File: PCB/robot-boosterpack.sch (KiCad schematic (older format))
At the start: 33 parts

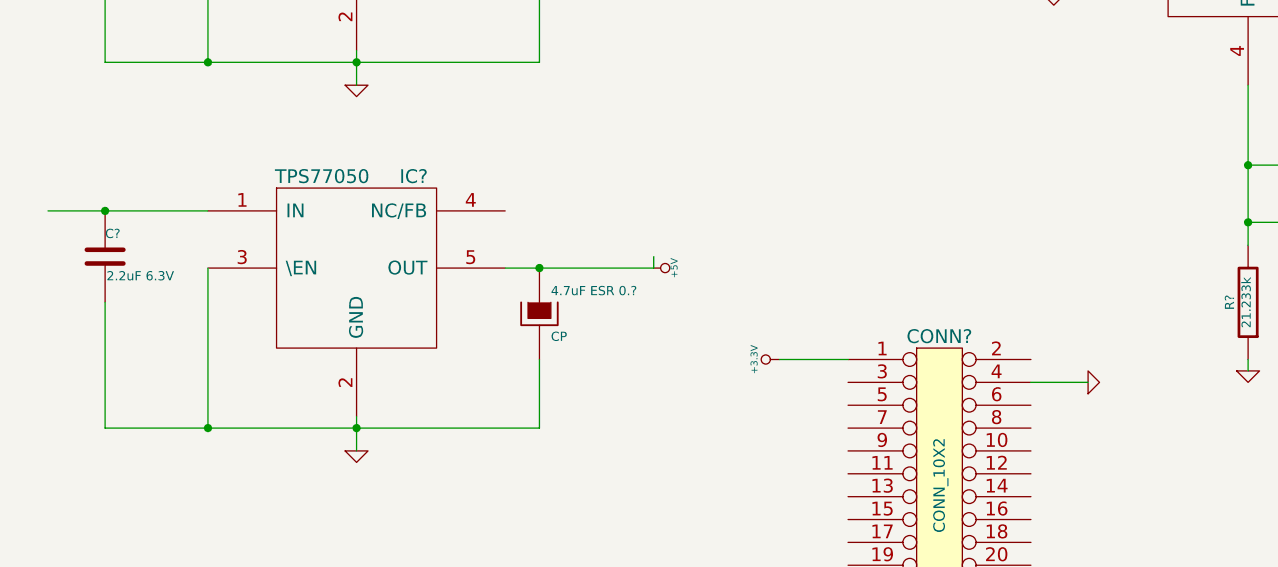
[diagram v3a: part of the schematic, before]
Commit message: updated 5V regulator circuit
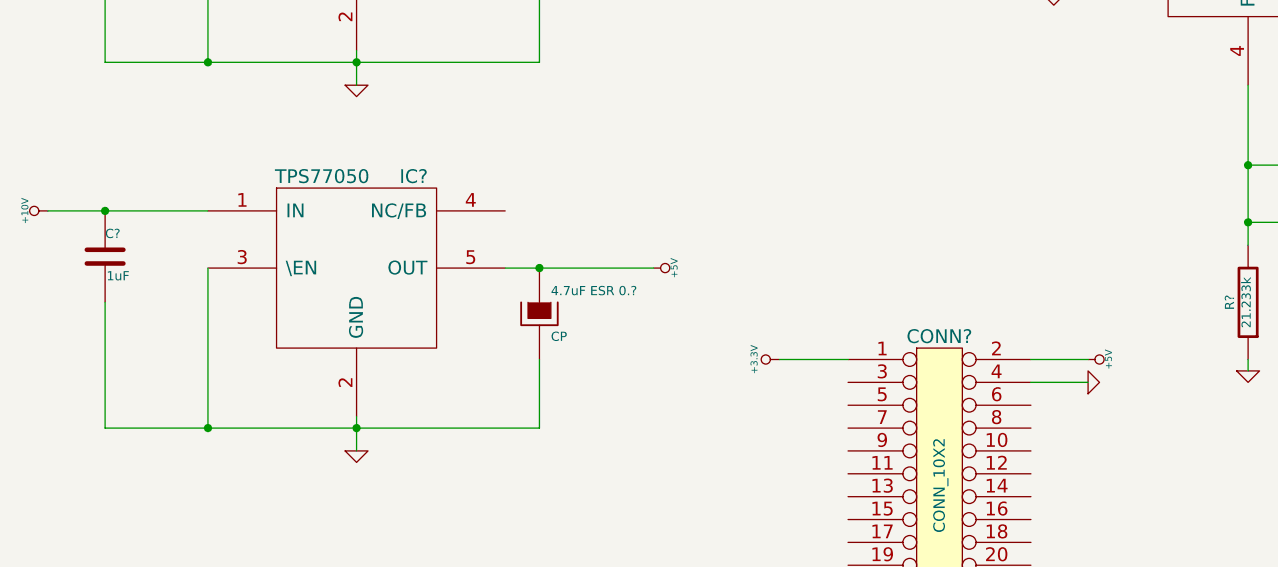
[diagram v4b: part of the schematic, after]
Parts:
- C?: value 2.2uF 6.3V -> 1uF
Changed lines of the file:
@@
 P 950 2700
 F 0 "C?" H 950 2800 40  0000 L CNN
-F 1 "2.2uF 6.3V" H 956 2615 40  0000 L CNN
+F 1 "1uF" H 956 2615 40  0000 L CNN
 F 2 "~" H 988 2550 30  0000 C CNN
 F 3 "~" H 950 2700 60  0000 C CNN
@@
 	0    1    1    0
 $EndComp
-Wire Wire Line
-	3350 2750 3350 2700
 Connection ~ 2850 2750
 Connection ~ 950  900
 Connection ~ 2850 1150
+$Comp
+L +5V #PWR?
+U 1 1 53AA0197
+P 5250 3150
+F 0 "#PWR?" H 5250 3240 20  0001 C CNN
+F 1 "+5V" H 5250 3240 30  0000 C CNN
+F 2 "" H 5250 3150 60  0000 C CNN
+F 3 "" H 5250 3150 60  0000 C CNN
+	1    5250 3150
+	0    1    1    0
+$EndComp
+Wire Wire Line
+	5000 3150 5250 3150
+$Comp
+L +10V #PWR?
+U 1 1 53AA074A
+P 700 2500
+F 0 "#PWR?" H 700 2450 20  0001 C CNN
+F 1 "+10V" H 700 2600 30  0000 C CNN
+F 2 "" H 700 2500 60  0000 C CNN
+F 3 "" H 700 2500 60  0000 C CNN
+	1    700  2500
+	0    -1   -1   0
+$EndComp
 $EndSCHEMATC

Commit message: updated 5V regulator capacitor values
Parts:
- removed 4.7uF~ESR~0.?: CP, symbol CP
- added C?: 4.7uF ESR 0.2, symbol CP
- C?: renamed from 4.7uF; value CP -> 4.7uF ESR 0.2
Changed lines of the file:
@@
 $EndComp
 $Comp
-L CP 4.7uF
+L CP C?
 U 1 1 53A8B338
 P 2850 1350
-F 0 "4.7uF ESR 0.2" H 2900 1450 40  0000 L CNN
-F 1 "CP" H 2900 1250 40  0000 L CNN
+F 0 "C?" H 2900 1450 40  0000 L CNN
+F 1 "4.7uF ESR 0.2" H 2900 1250 40  0000 L CNN
 F 2 "" H 2950 1200 30  0000 C CNN
 F 3 "" H 2850 1350 300 0000 C CNN
@@
 	1    0    0    -1
 $EndComp
-$Comp
-L CP 4.7uF~ESR~0.?
-U 1 1 53A9EE61
-P 2850 2950
-F 0 "4.7uF ESR 0.?" H 2900 3050 40  0000 L CNN
-F 1 "CP" H 2900 2850 40  0000 L CNN
-F 2 "" H 2950 2800 30  0000 C CNN
-F 3 "" H 2850 2950 300 0000 C CNN
-	1    2850 2950
-	1    0    0    -1
-$EndComp
 Wire Wire Line
 	1400 2500 700  2500
@@
 	0    -1   -1   0
 $EndComp
+$Comp
+L CP C?
+U 1 1 53AA20BE
+P 2850 2950
+F 0 "C?" H 2900 3050 40  0000 L CNN
+F 1 "4.7uF ESR 0.2" H 2900 2850 40  0000 L CNN
+F 2 "" H 2950 2800 30  0000 C CNN
+F 3 "" H 2850 2950 300 0000 C CNN
+	1    2850 2950
+	1    0    0    -1
+$EndComp
 $EndSCHEMATC

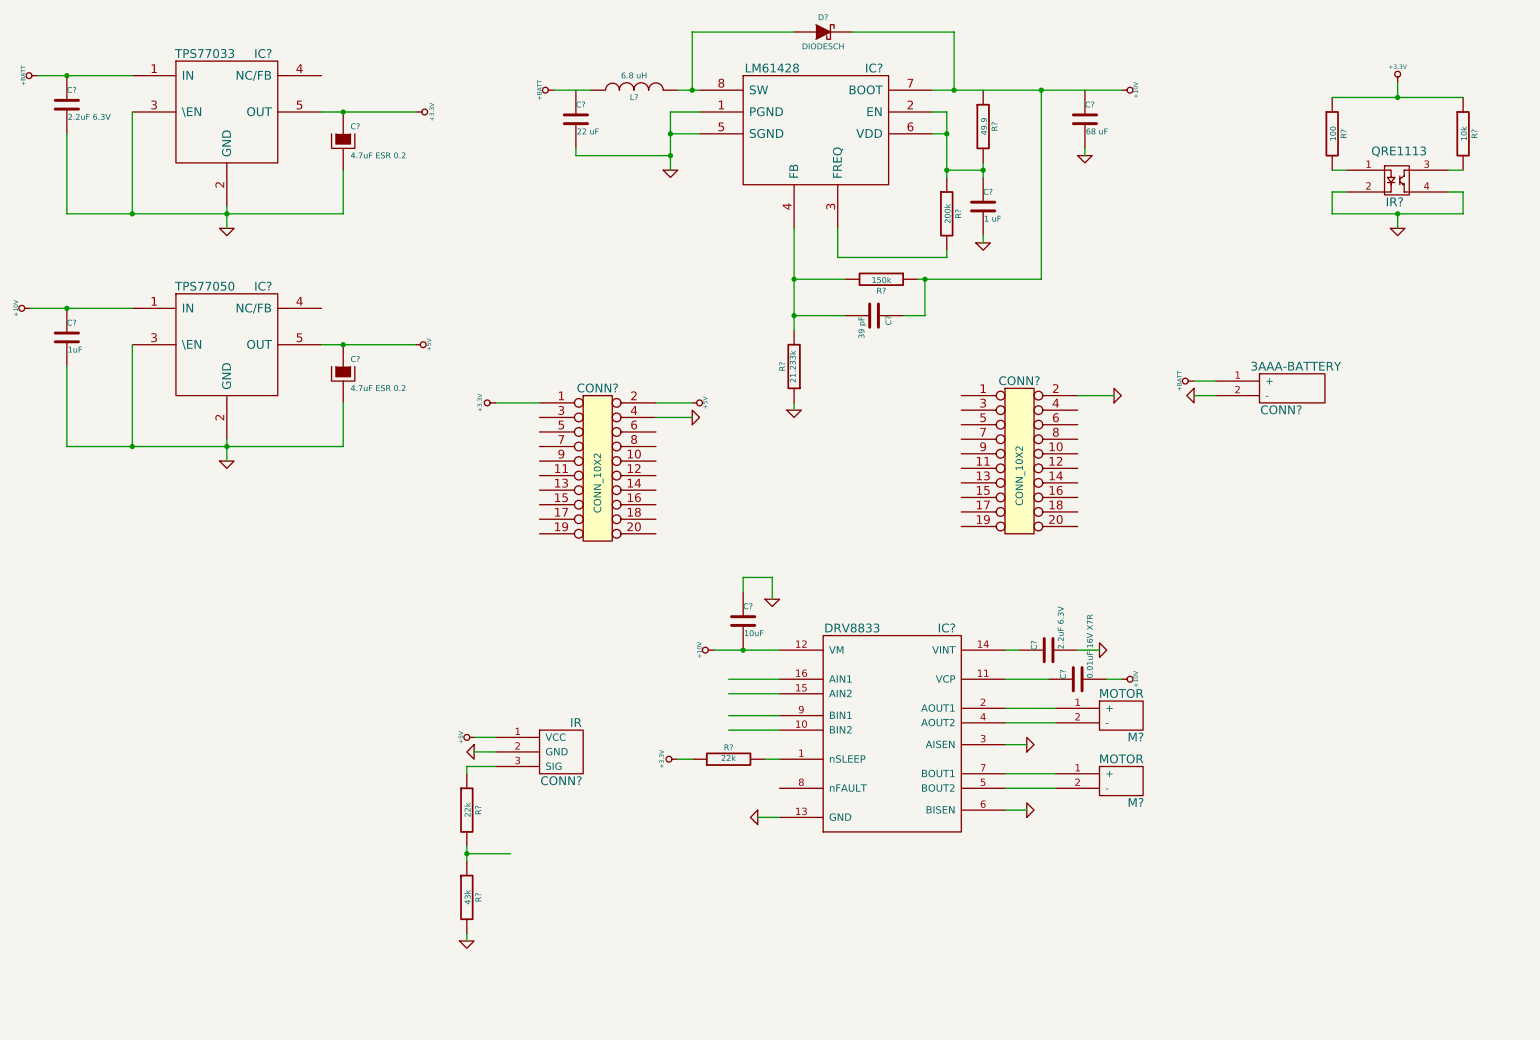
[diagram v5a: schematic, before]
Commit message: added servo connectors
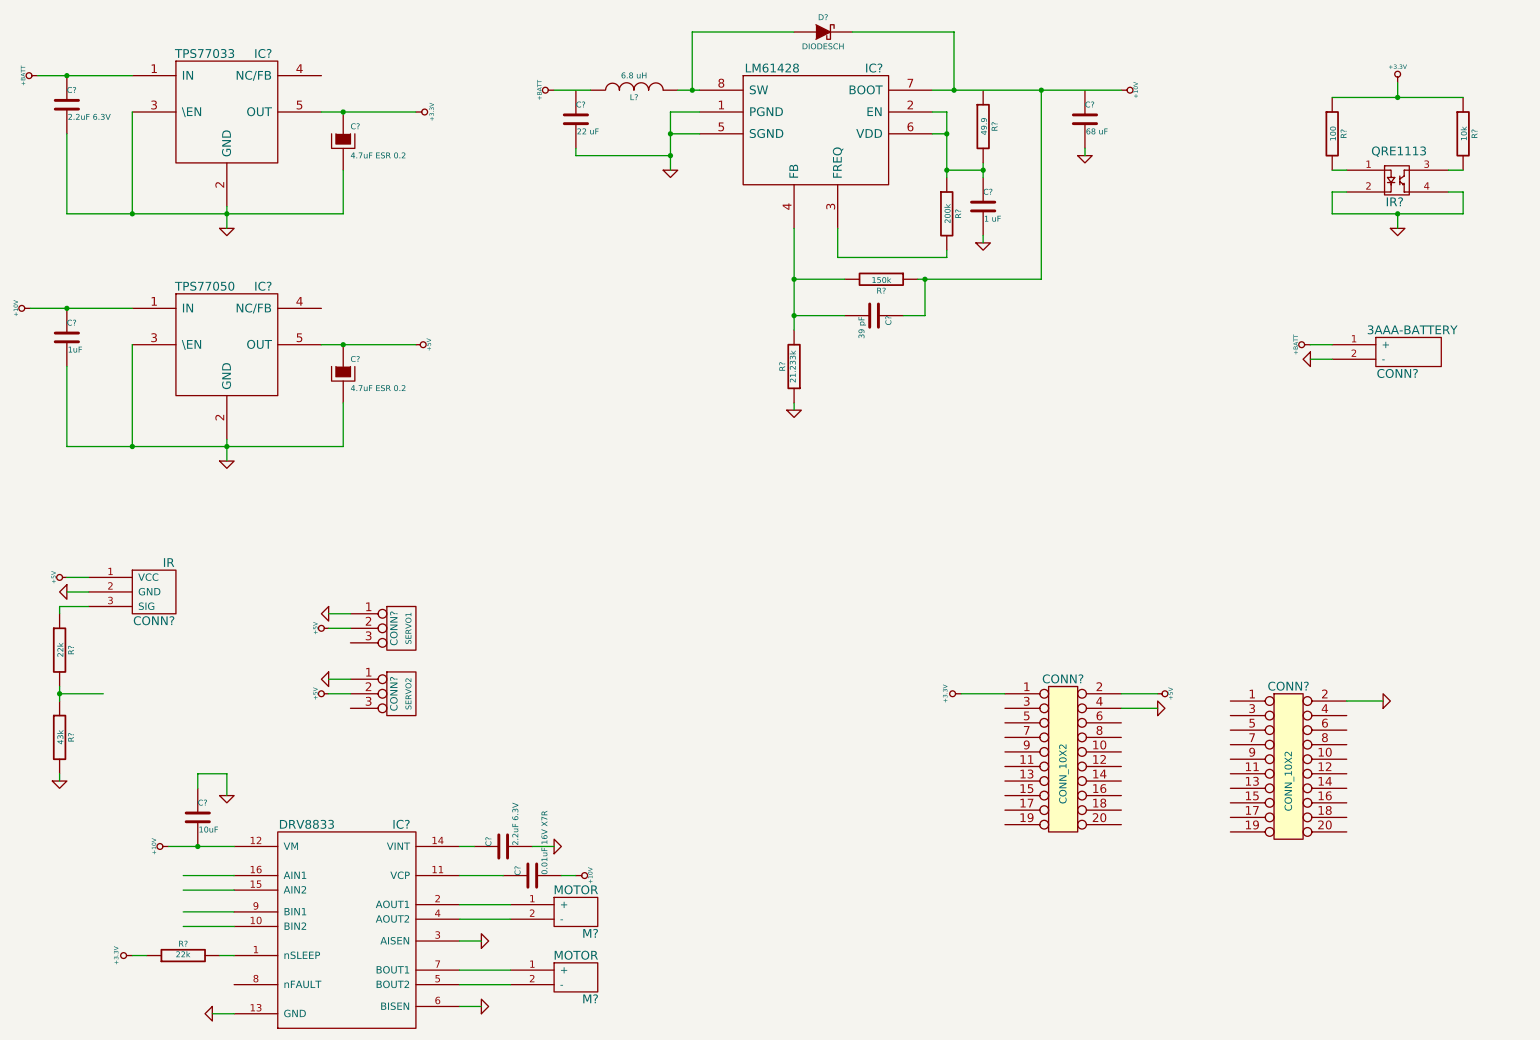
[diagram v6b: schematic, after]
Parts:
- added CONN?: SERVO2, symbol CONN_3
- added CONN?: SERVO1, symbol CONN_3
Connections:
- wire segments 88 -> 92
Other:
- moved on the sheet: C?, CONN?, IC?, M?, R?

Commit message: created boosterpack connections
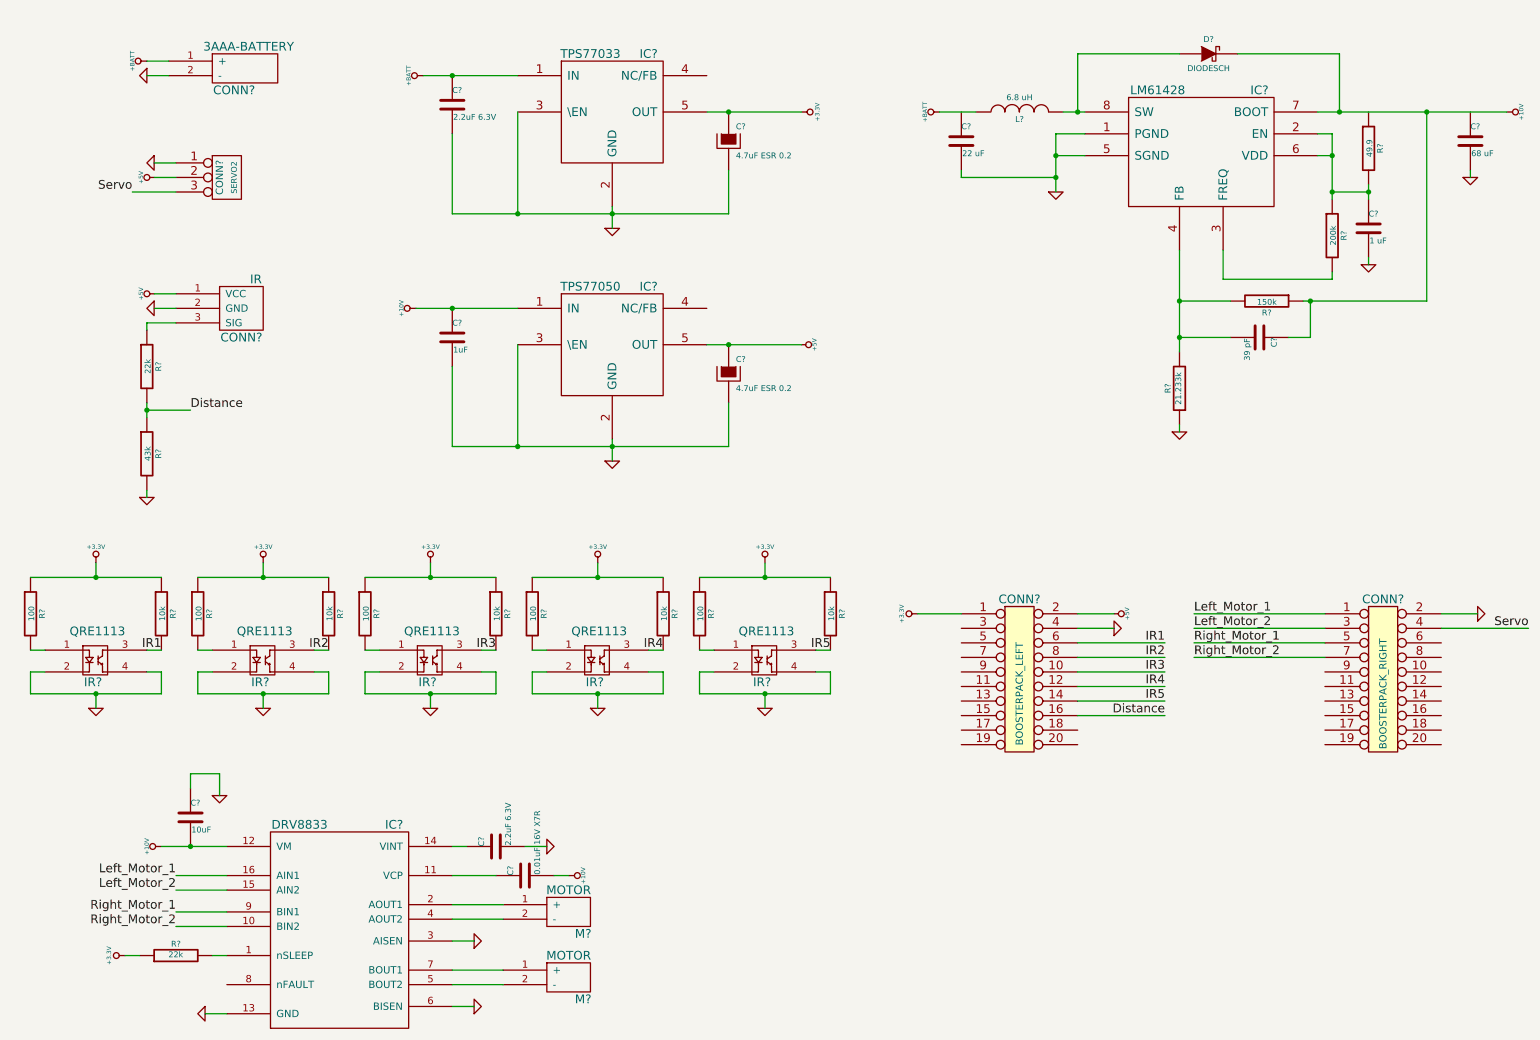
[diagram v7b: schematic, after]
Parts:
- removed CONN?: SERVO1, symbol CONN_3
- added IR? (x4): QRE1113, ~, symbol QRE1113
- added R? (x4): 100, ~, symbol R
- added R? (x4): 10k, ~, symbol R
- CONN?: value CONN_10X2 -> BOOSTERPACK_LEFT
- CONN?: value CONN_10X2 -> BOOSTERPACK_RIGHT
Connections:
- net labels added: Distance, IR1, IR2, IR3, IR4, IR5, Left_Motor_1, Left_Motor_2, Right_Motor_1, Right_Motor_2, Servo
- wire segments 92 -> 142
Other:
- moved on the sheet: C?, CONN?, D?, IC?, IR?, L?, M?, R?

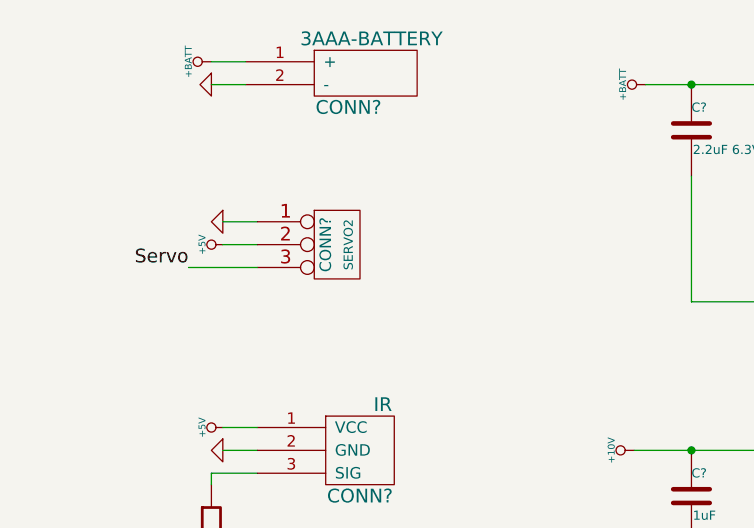
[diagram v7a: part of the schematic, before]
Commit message: updated servo connector label
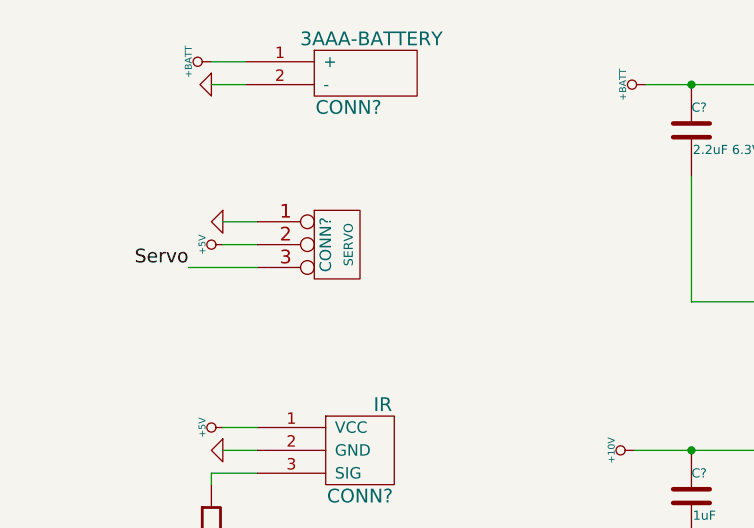
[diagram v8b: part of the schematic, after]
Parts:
- CONN?: value SERVO2 -> SERVO
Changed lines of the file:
@@
 P 2050 1600
 F 0 "CONN?" V 2000 1600 50  0000 C CNN
-F 1 "SERVO2" V 2100 1600 40  0000 C CNN
+F 1 "SERVO" V 2100 1600 40  0000 C CNN
 F 2 "" H 2050 1600 60  0000 C CNN
 F 3 "" H 2050 1600 60  0000 C CNN
